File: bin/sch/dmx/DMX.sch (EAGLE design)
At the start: 7 parts, among them U1 MAX485, U2 6N137

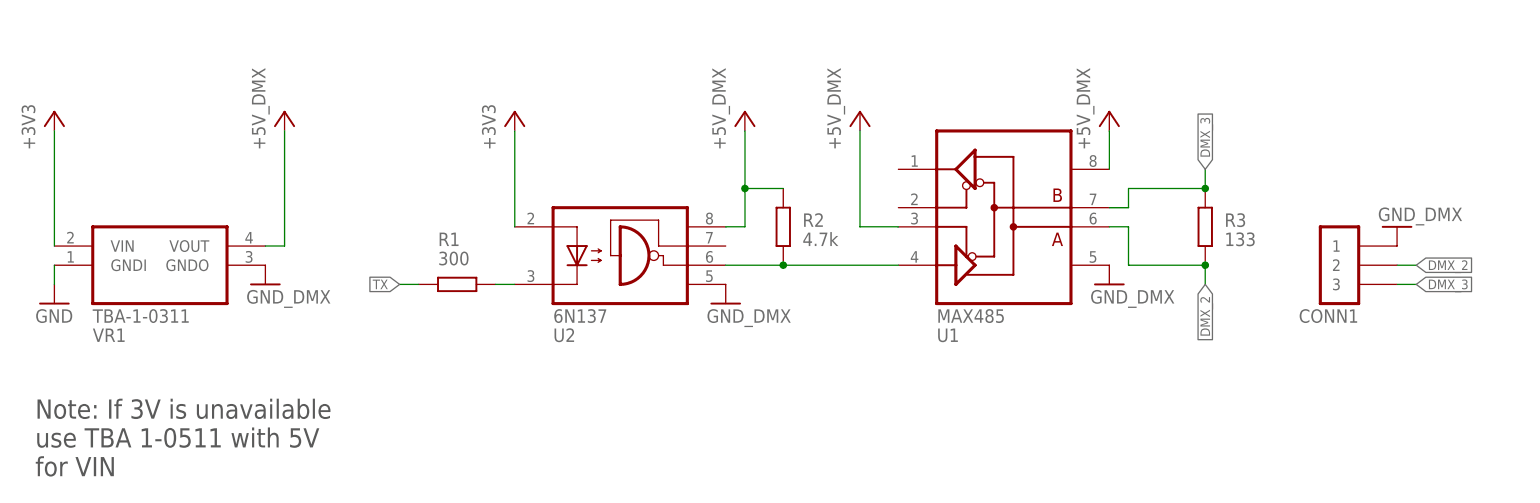
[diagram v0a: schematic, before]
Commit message: update dmx schematic
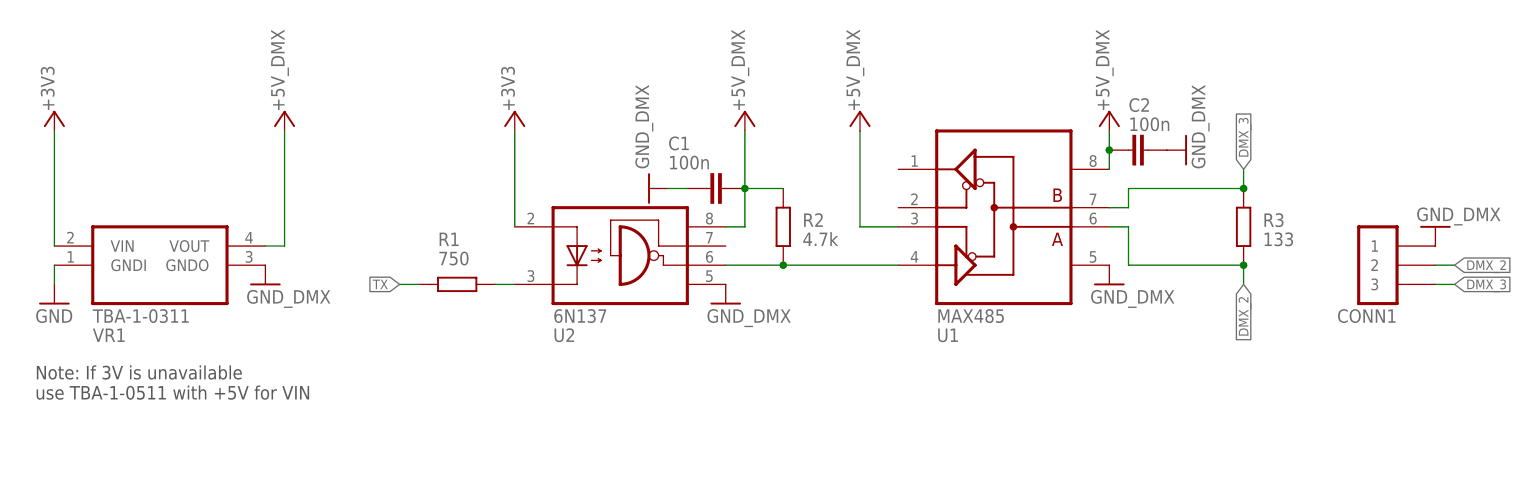
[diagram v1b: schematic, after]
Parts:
- added C1, C2: 100n, igor_lbr:CAPACITOR-0805
- R1: value 300 -> 750
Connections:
- net +5V_DMX: now also C1.2, C2.1
- net GND: now also C1.1, C2.2
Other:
- note added: "Note: If 3V is unavailable use TBA-1-0511 with +5V for VIN"
- note removed: "Note: If 3V is unavailable use TBA 1-0511 with 5V for VIN"
- moved on the sheet: CONN1, R3
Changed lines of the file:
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@@
 <part name="P+1" library="supply1" deviceset="+5V" device="" value="+5V_DMX"/>
 <part name="U2" library="igor_lbr" deviceset="6N137" device=""/>
-<part name="R1" library="igor_lbr" deviceset="RESISTOR" device="-0805" value="300"/>
+<part name="R1" library="igor_lbr" deviceset="RESISTOR" device="-0805" value="750"/>
 <part name="R2" library="igor_lbr" deviceset="RESISTOR" device="-0805" value="4.7k"/>
 <part name="P+3" library="supply1" deviceset="+5V" device="" value="+5V_DMX"/>
@@
 <part name="GND5" library="supply1" deviceset="GND" device="" value="GND_DMX"/>
 <part name="P+2" library="supply1" deviceset="+5V" device="" value="+5V_DMX"/>
+<part name="C1" library="igor_lbr" deviceset="CAPACITOR" device="-0805" value="100n"/>
+<part name="GND_DMX1" library="supply1" deviceset="GND" device="" value="GND_DMX"/>
+<part name="C2" library="igor_lbr" deviceset="CAPACITOR" device="-0805" value="100n"/>
+<part name="GND3" library="supply1" deviceset="GND" device="" value="GND_DMX"/>
 </parts>
 <sheets>
 <sheet>
 <plain>
-<text x="-78.74" y="45.72" size="2.54" layer="97">Note: If 3V is unavailable
-use TBA 1-0511 with 5V
-for VIN</text>
+<text x="-78.74" y="55.88" size="1.778" layer="97">Note: If 3V is unavailable
+use TBA-1-0511 with +5V for VIN</text>
 </plain>
 <instances>
 <instance part="U1" gate="G$1" x="40.64" y="68.58"/>
-<instance part="R3" gate="G$1" x="76.2" y="78.74" smashed="yes" rot="R270">
-<attribute name="NAME" x="78.74" y="78.74" size="1.778" layer="95" font="vector"/>
-<attribute name="VALUE" x="78.74" y="76.2" size="1.778" layer="96" font="vector"/>
+<instance part="R3" gate="G$1" x="81.28" y="78.74" smashed="yes" rot="R270">
+<attribute name="NAME" x="83.82" y="78.74" size="1.778" layer="95" font="vector"/>
+<attribute name="VALUE" x="83.82" y="76.2" size="1.778" layer="96" font="vector"/>
 </instance>
 <instance part="GND2" gate="1" x="63.5" y="71.12" smashed="yes">
 <attribute name="VALUE" x="60.96" y="68.58" size="1.778" layer="96"/>
 </instance>
-<instance part="P+1" gate="1" x="63.5" y="93.98"/>
+<instance part="P+1" gate="1" x="63.5" y="93.98" smashed="yes">
+<attribute name="VALUE" x="63.5" y="93.98" size="1.778" layer="96" rot="R90"/>
+</instance>
 <instance part="U2" gate="G$1" x="-10.16" y="68.58"/>
 <instance part="R1" gate="G$1" x="-22.86" y="71.12" smashed="yes">
@@
 <attribute name="VALUE" x="22.86" y="76.2" size="1.778" layer="96" font="vector"/>
 </instance>
-<instance part="P+3" gate="1" x="15.24" y="93.98"/>
-<instance part="CONN1" gate="G$1" x="96.52" y="68.58" rot="MR0"/>
-<instance part="GND1" gate="1" x="101.6" y="78.74" smashed="yes" rot="MR180">
-<attribute name="VALUE" x="99.06" y="81.28" size="1.778" layer="96" rot="MR180"/>
+<instance part="P+3" gate="1" x="15.24" y="93.98" smashed="yes">
+<attribute name="VALUE" x="15.24" y="93.98" size="1.778" layer="96" rot="R90"/>
+</instance>
+<instance part="CONN1" gate="G$1" x="101.6" y="68.58" rot="MR0"/>
+<instance part="GND1" gate="1" x="106.68" y="78.74" smashed="yes" rot="MR180">
+<attribute name="VALUE" x="104.14" y="81.28" size="1.778" layer="96" rot="MR180"/>
 </instance>
 <instance part="GND_DMX" gate="1" x="12.7" y="68.58" smashed="yes">
@@
 <instance part="VR1" gate="G$1" x="-71.12" y="68.58"/>
 <instance part="GND4" gate="1" x="-76.2" y="68.58"/>
-<instance part="+3V1" gate="G$1" x="-76.2" y="93.98"/>
-<instance part="P+4" gate="1" x="-45.72" y="93.98"/>
-<instance part="+3V2" gate="G$1" x="-15.24" y="93.98"/>
+<instance part="+3V1" gate="G$1" x="-76.2" y="93.98" smashed="yes">
+<attribute name="VALUE" x="-76.2" y="93.98" size="1.778" layer="96" rot="R90"/>
+</instance>
+<instance part="P+4" gate="1" x="-45.72" y="93.98" smashed="yes">
+<attribute name="VALUE" x="-45.72" y="93.98" size="1.778" layer="96" rot="R90"/>
+</instance>
+<instance part="+3V2" gate="G$1" x="-15.24" y="93.98" smashed="yes">
+<attribute name="VALUE" x="-15.24" y="93.98" size="1.778" layer="96" rot="R90"/>
+</instance>
 <instance part="GND5" gate="1" x="-48.26" y="71.12" smashed="yes">
 <attribute name="VALUE" x="-50.8" y="68.58" size="1.778" layer="96"/>
 </instance>
-<instance part="P+2" gate="1" x="30.48" y="93.98"/>
+<instance part="P+2" gate="1" x="30.48" y="93.98" smashed="yes">
+<attribute name="VALUE" x="30.48" y="93.98" size="1.778" layer="96" rot="R90"/>
+</instance>
+<instance part="C1" gate="C" x="12.7" y="83.82" smashed="yes" rot="R90">
+<attribute name="NAME" x="5.08" y="88.9" size="1.778" layer="95" font="vector"/>
+<attribute name="VALUE" x="5.08" y="86.36" size="1.778" layer="96" font="vector"/>
+</instance>
+<instance part="GND_DMX1" gate="1" x="2.54" y="83.82" smashed="yes" rot="R270">
+<attribute name="VALUE" x="2.54" y="86.36" size="1.778" layer="96" rot="R90"/>
+</instance>
+<instance part="C2" gate="C" x="68.58" y="88.9" smashed="yes" rot="R90">
+<attribute name="NAME" x="66.04" y="93.98" size="1.778" layer="95" font="vector"/>
+<attribute name="VALUE" x="66.04" y="91.44" size="1.778" layer="96" font="vector"/>
+</instance>
+<instance part="GND3" gate="1" x="73.66" y="88.9" smashed="yes" rot="R90">
+<attribute name="VALUE" x="76.2" y="86.36" size="1.778" layer="96" rot="R90"/>
+</instance>
 </instances>
 <busses>
@@
 <wire x1="66.04" y1="81.28" x2="66.04" y2="83.82" width="0.1524" layer="91"/>
 <pinref part="R3" gate="G$1" pin="1"/>
-<wire x1="66.04" y1="83.82" x2="76.2" y2="83.82" width="0.1524" layer="91"/>
-<wire x1="76.2" y1="83.82" x2="76.2" y2="86.36" width="0.1524" layer="91"/>
-<junction x="76.2" y="83.82"/>
-<label x="76.2" y="86.36" size="1.27" layer="95" rot="R90" xref="yes"/>
+<wire x1="66.04" y1="83.82" x2="81.28" y2="83.82" width="0.1524" layer="91"/>
+<wire x1="81.28" y1="83.82" x2="81.28" y2="86.36" width="0.1524" layer="91"/>
+<junction x="81.28" y="83.82"/>
+<label x="81.28" y="86.36" size="1.27" layer="95" rot="R90" xref="yes"/>
 </segment>
 <segment>
 <pinref part="CONN1" gate="G$1" pin="3"/>
-<wire x1="101.6" y1="71.12" x2="104.14" y2="71.12" width="0.1524" layer="91"/>
-<label x="104.14" y="71.12" size="1.27" layer="95" rot="MR180" xref="yes"/>
+<wire x1="106.68" y1="71.12" x2="109.22" y2="71.12" width="0.1524" layer="91"/>
+<label x="109.22" y="71.12" size="1.27" layer="95" rot="MR180" xref="yes"/>
 </segment>
 </net>
@@
 <wire x1="66.04" y1="78.74" x2="66.04" y2="73.66" width="0.1524" layer="91"/>
 <pinref part="R3" gate="G$1" pin="2"/>
-<wire x1="66.04" y1="73.66" x2="76.2" y2="73.66" width="0.1524" layer="91"/>
-<wire x1="76.2" y1="73.66" x2="76.2" y2="71.12" width="0.1524" layer="91"/>
-<junction x="76.2" y="73.66"/>
-<label x="76.2" y="71.12" size="1.27" layer="95" rot="R270" xref="yes"/>
+<wire x1="66.04" y1="73.66" x2="81.28" y2="73.66" width="0.1524" layer="91"/>
+<wire x1="81.28" y1="73.66" x2="81.28" y2="71.12" width="0.1524" layer="91"/>
+<junction x="81.28" y="73.66"/>
+<label x="81.28" y="71.12" size="1.27" layer="95" rot="R270" xref="yes"/>
 </segment>
 <segment>
 <pinref part="CONN1" gate="G$1" pin="2"/>
-<wire x1="101.6" y1="73.66" x2="104.14" y2="73.66" width="0.1524" layer="91"/>
-<label x="104.14" y="73.66" size="1.27" layer="95" rot="MR180" xref="yes"/>
+<wire x1="106.68" y1="73.66" x2="109.22" y2="73.66" width="0.1524" layer="91"/>
+<label x="109.22" y="73.66" size="1.27" layer="95" rot="MR180" xref="yes"/>
 </segment>
 </net>
@@
 <wire x1="-76.2" y1="71.12" x2="-76.2" y2="73.66" width="0.1524" layer="91"/>
 </segment>
+<segment>
+<pinref part="C1" gate="C" pin="1"/>
+<pinref part="GND_DMX1" gate="1" pin="GND"/>
+<wire x1="5.08" y1="83.82" x2="7.62" y2="83.82" width="0.1524" layer="91"/>
+</segment>
+<segment>
+<pinref part="C2" gate="C" pin="2"/>
+<pinref part="GND3" gate="1" pin="GND"/>
+</segment>
 </net>
 <net name="+5V_DMX" class="0">
@@
 <pinref part="U1" gate="G$1" pin="VCC"/>
 <pinref part="P+1" gate="1" pin="+5V"/>
-<wire x1="63.5" y1="86.36" x2="63.5" y2="91.44" width="0.1524" layer="91"/>
+<wire x1="63.5" y1="86.36" x2="63.5" y2="88.9" width="0.1524" layer="91"/>
+<pinref part="C2" gate="C" pin="1"/>
+<wire x1="63.5" y1="88.9" x2="63.5" y2="91.44" width="0.1524" layer="91"/>
+<junction x="63.5" y="88.9"/>
 </segment>
 <segment>
@@
 <wire x1="20.32" y1="83.82" x2="15.24" y2="83.82" width="0.1524" layer="91"/>
 <junction x="15.24" y="83.82"/>
+<pinref part="C1" gate="C" pin="2"/>
 </segment>
 <segment>
